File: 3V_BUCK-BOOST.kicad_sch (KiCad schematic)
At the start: 9 parts

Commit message: footprint assignments gedaan + verbeteringen
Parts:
- removed L?: L, symbol Device:L
- added L3: DFE18SAN1R0ME0L, DFE18SAN1R0ME0L, symbol SamacSys_Parts:DFE18SAN1R0ME0L
- C? (x2): footprint (none) -> Capacitor_SMD:C_0805_2012Metric_Pad1.18x1.45mm_HandSolder
- J?: footprint (none) -> Connector_PinHeader_2.54mm:PinHeader_1x03_P2.54mm_Vertical
- R? (x4): footprint (none) -> Resistor_SMD:R_0805_2012Metric_Pad1.20x1.40mm_HandSolder
- U?: footprint SOTFL50P160X60-8N -> SamacSys_Parts:SOTFL50P160X60-8N
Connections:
- net at U?.2 (LX2): now also L3.2
- net at U?.3 (LX1): now also L3.1
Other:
- note added: "mode = 0 ; PFM operating mode mode = 1 ; PWM operating mode"
- moved on the sheet: R?

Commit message: aantal componenten veranderd.
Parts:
- removed L3: DFE18SAN1R0ME0L, DFE18SAN1R0ME0L, symbol SamacSys_Parts:DFE18SAN1R0ME0L
- removed U?: TPS631000DRLR, SamacSys_Parts:SOTFL50P160X60-8N, symbol SamacSys_Parts:TPS631000DRLR
- added L2: DFE18SAN1R0ME0L, Components:DFE18SAN1R0ME0L, symbol CustomSymbols:DFE18SAN1R0ME0L
- added U4: TPS631000DRLR, Components:SOTFL50P160X60-8N, symbol CustomSymbols:TPS631000DRLR
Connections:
- net +3V0: now also U4.1 (VOUT)
- net +BATT: now also U4.4 (VIN)
- net GND: now also U4.7 (GND)
- net at R?.1: now also U4.5 (EN)
- net at R?.2: now also U4.6 (MODE)
- net at R?.1, R?.2: now also U4.8 (FB)
- new net: L2.1, U4.3 (LX1)
- new net: L2.2, U4.2 (LX2)

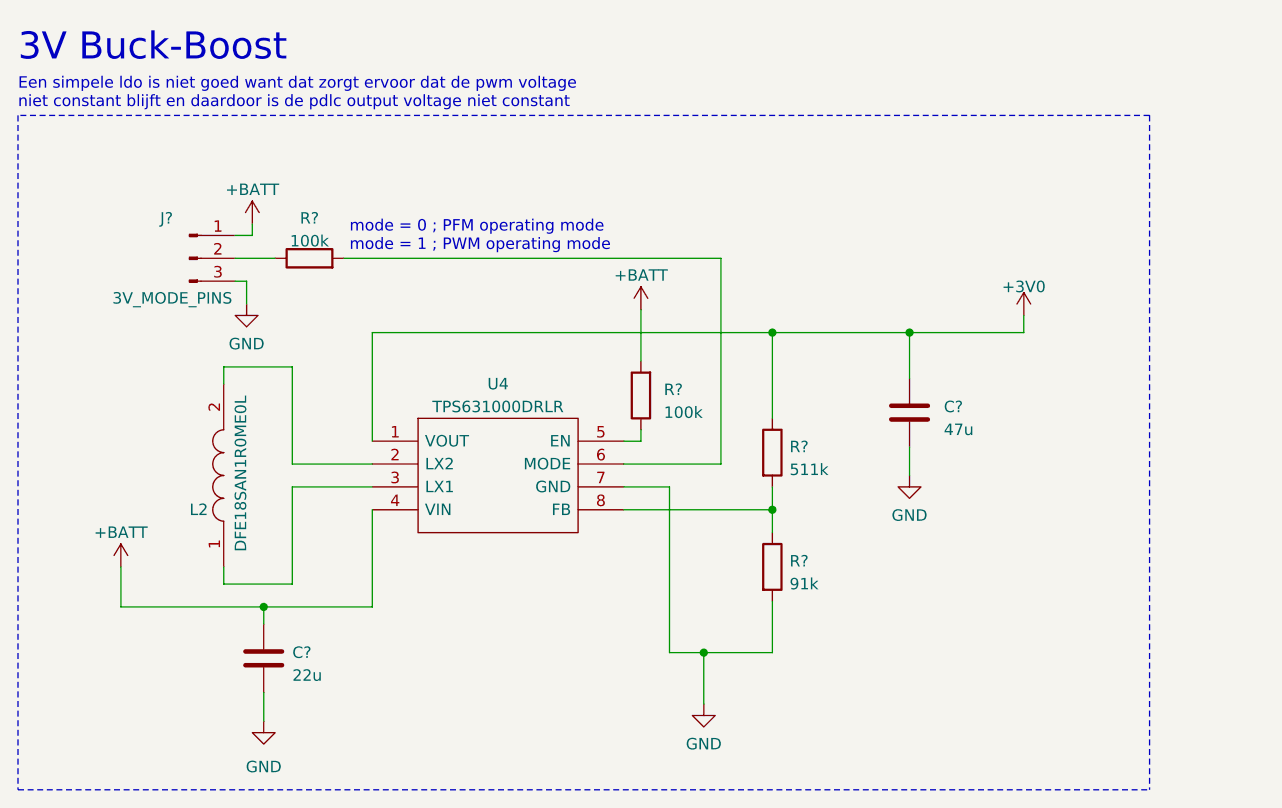
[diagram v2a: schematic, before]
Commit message: Kleine veranderingen gebaseerd op feedback whatsapp
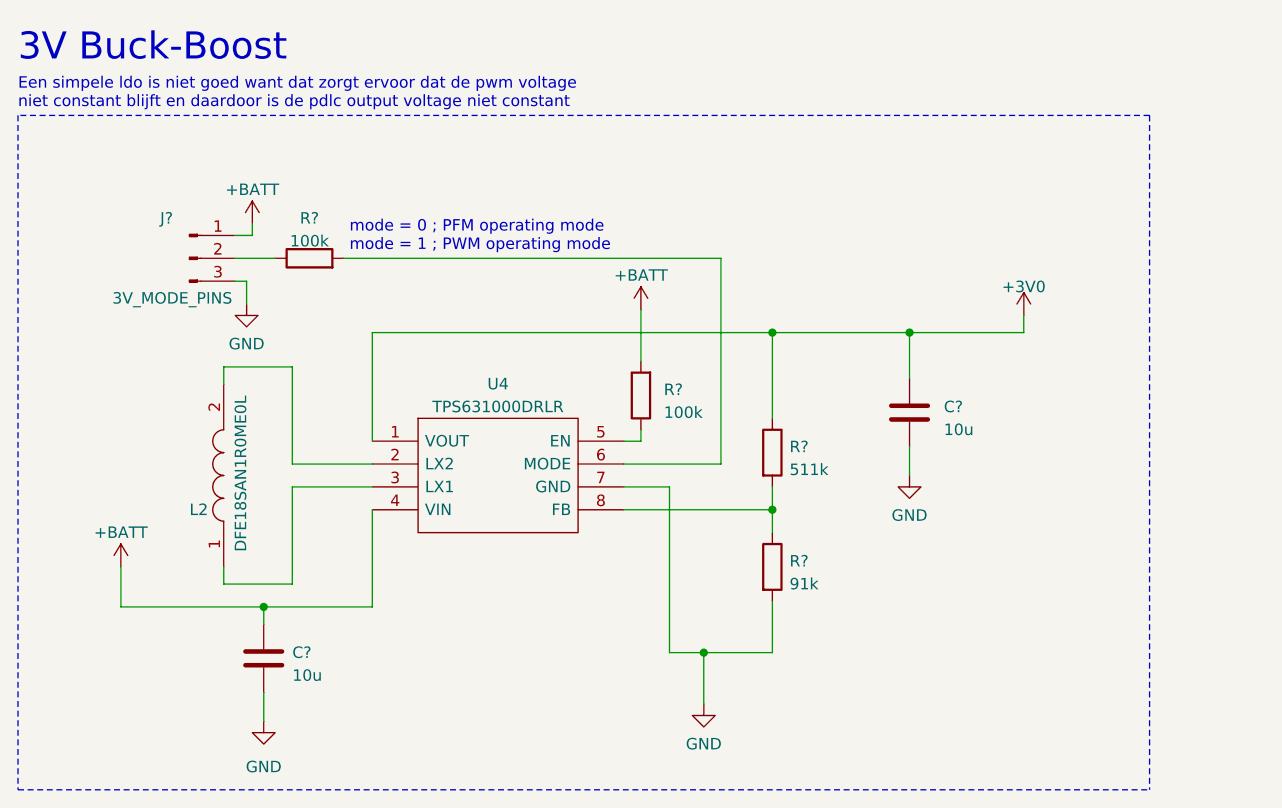
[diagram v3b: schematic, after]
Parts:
- C?: value 22u -> 10u
- C?: value 47u -> 10u
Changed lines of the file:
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@@
       (effects (font (size 1.27 1.27)) (justify left))
     )
-    (property "Value" "22u" (at 82.55 103.505 0)
+    (property "Value" "10u" (at 82.55 103.505 0)
       (effects (font (size 1.27 1.27)) (justify left))
     )
@@
       (effects (font (size 1.27 1.27)) (justify left))
     )
-    (property "Value" "47u" (at 154.94 76.2 0)
+    (property "Value" "10u" (at 154.94 76.2 0)
       (effects (font (size 1.27 1.27)) (justify left))
     )

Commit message: PCBv2.01
Eerste versie van de tweede versie van de pcb prototype.
Nieuwe PDLC voeding, extra pinnen beschikbaar voor GUI inclusief voeding pinnen.
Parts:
- removed J?: 3V_MODE_PINS, Connector_PinHeader_2.54mm:PinHeader_1x03_P2.54mm_Vertical, symbol Connector:Conn_01x03_Pin
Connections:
- net +BATT: now also R?.1
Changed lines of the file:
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@@
-    (stroke (width 0) (type default))
-  )
-  (wire (pts (xy 76.2 59.69) (xy 77.47 59.69))
     (stroke (width 0) (type default))
   )
@@
     (stroke (width 0) (type default))
   )
-  (wire (pts (xy 76.2 57.15) (xy 80.645 57.15))
+  (wire (pts (xy 77.47 57.15) (xy 80.645 57.15))
     (stroke (width 0) (type default))
   )
@@
     (stroke (width 0) (type default))
   )
-  (wire (pts (xy 78.105 53.34) (xy 78.105 54.61))
+  (wire (pts (xy 77.47 53.34) (xy 77.47 57.15))
     (stroke (width 0) (type default))
   )
@@
     (stroke (width 0) (type default))
   )
-  (wire (pts (xy 78.105 54.61) (xy 76.2 54.61))
-    (stroke (width 0) (type default))
-  )
   (wire (pts (xy 88.265 57.15) (xy 130.175 57.15))
-    (stroke (width 0) (type default))
-  )
-  (wire (pts (xy 77.47 59.69) (xy 77.47 62.23))
     (stroke (width 0) (type default))
   )
@@
   )
   (text "mode = 0 ; PFM operating mode\nmode = 1 ; PWM operating mode"
-    (at 88.9 56.515 0)
+    (at 88.9 57.15 0)
     (effects (font (size 1.27 1.27)) (justify left bottom))
   )
@@
         (path "/5dc439a9-720d-4bdc-b61f-78a76fde4df5/b5328c87-500d-46a7-aecc-989117275688"
           (reference "#PWR053") (unit 1)
-        )
-      )
-    )
-  )
-  (symbol (lib_id "Connector:Conn_01x03_Pin") (at 71.12 57.15 0) (unit 1)
-    (in_bom yes) (on_board yes) (dnp no)
-    (property "Reference" "J?" (at 68.58 52.705 0)
-      (effects (font (size 1.27 1.27)))
-    )
-    (property "Value" "3V_MODE_PINS" (at 69.215 61.595 0)
-      (effects (font (size 1.27 1.27)))
-    )
-    (property "Footprint" "Connector_PinHeader_2.54mm:PinHeader_1x03_P2.54mm_Vertical" (at 71.12 57.15 0)
-      (effects (font (size 1.27 1.27)) hide)
-    )
-    (property "Datasheet" "~" (at 71.12 57.15 0)
-      (effects (font (size 1.27 1.27)) hide)
-    )
-    (pin "1")
-    (pin "2")
-    (pin "3")
-    (instances
-      (project "RookBril"
-        (path "/5dc439a9-720d-4bdc-b61f-78a76fde4df5/2d26b15a-54d8-4f7d-a410-dc25ffe321a1"
-          (reference "J?") (unit 1)
-        )
-        (path "/5dc439a9-720d-4bdc-b61f-78a76fde4df5/b5328c87-500d-46a7-aecc-989117275688"
-          (reference "J13") (unit 1)
         )
       )
@@
     )
   )
-  (symbol (lib_id "power:+BATT") (at 78.105 53.34 0) (unit 1)
-    (in_bom yes) (on_board yes) (dnp no) (fields_autoplaced)
-    (property "Reference" "#PWR?" (at 78.105 57.15 0)
-      (effects (font (size 1.27 1.27)) hide)
-    )
-    (property "Value" "+BATT" (at 78.105 49.53 0)
-      (effects (font (size 1.27 1.27)))
-    )
-    (property "Footprint" "" (at 78.105 53.34 0)
-      (effects (font (size 1.27 1.27)) hide)
-    )
-    (property "Datasheet" "" (at 78.105 53.34 0)
+  (symbol (lib_id "power:+BATT") (at 77.47 53.34 0) (unit 1)
+    (in_bom yes) (on_board yes) (dnp no) (fields_autoplaced)
+    (property "Reference" "#PWR?" (at 77.47 57.15 0)
+      (effects (font (size 1.27 1.27)) hide)
+    )
+    (property "Value" "+BATT" (at 77.47 49.53 0)
+      (effects (font (size 1.27 1.27)))
+    )
+    (property "Footprint" "" (at 77.47 53.34 0)
+      (effects (font (size 1.27 1.27)) hide)
+    )
+    (property "Datasheet" "" (at 77.47 53.34 0)
       (effects (font (size 1.27 1.27)) hide)
     )
@@
         )
       )
-    )
-  )
-  (symbol (lib_id "power:GND") (at 77.47 62.23 0) (mirror y) (unit 1)
-    (in_bom yes) (on_board yes) (dnp no) (fields_autoplaced)
-    (property "Reference" "#PWR?" (at 77.47 68.58 0)
-      (effects (font (size 1.27 1.27)) hide)
-    )
-    (property "Value" "GND" (at 77.47 66.675 0)
-      (effects (font (size 1.27 1.27)))
-    )
-    (property "Footprint" "" (at 77.47 62.23 0)
-      (effects (font (size 1.27 1.27)) hide)
-    )
-    (property "Datasheet" "" (at 77.47 62.23 0)
-      (effects (font (size 1.27 1.27)) hide)
-    )
-    (pin "1")
-    (instances
-      (project "RookBril"
-        (path "/5dc439a9-720d-4bdc-b61f-78a76fde4df5/2d26b15a-54d8-4f7d-a410-dc25ffe321a1"
-          (reference "#PWR?") (unit 1)
-        )
-        (path "/5dc439a9-720d-4bdc-b61f-78a76fde4df5/b5328c87-500d-46a7-aecc-989117275688"
-          (reference "#PWR047") (unit 1)
-        )
-      )
